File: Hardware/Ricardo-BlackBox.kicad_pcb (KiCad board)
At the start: 4 copper layers, 45.1 x 35.1 mm, 83 parts, among them J1 RBUS, J2 USB_C_Receptacle_USB2.0, J3 Conn_01x08_Pin, U1 ESP32-S3, U2 SN65HVD230, U3 LM66200DRLR, U4 MAX77827AEFD+T, U5 SC4215ASTRT, U7 LM66200DRLR, Y1 R940000171

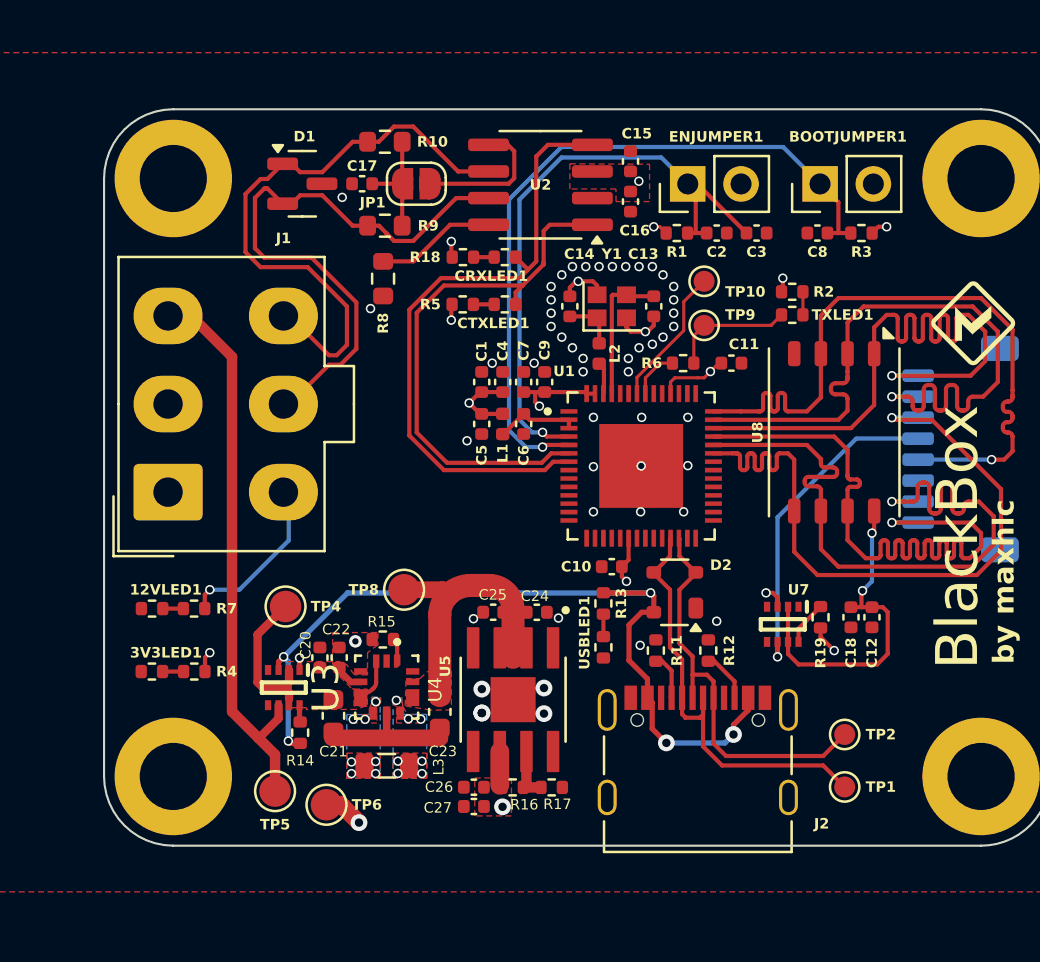
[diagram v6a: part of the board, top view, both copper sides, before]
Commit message: Update silkscreen labels for LEDs and pads
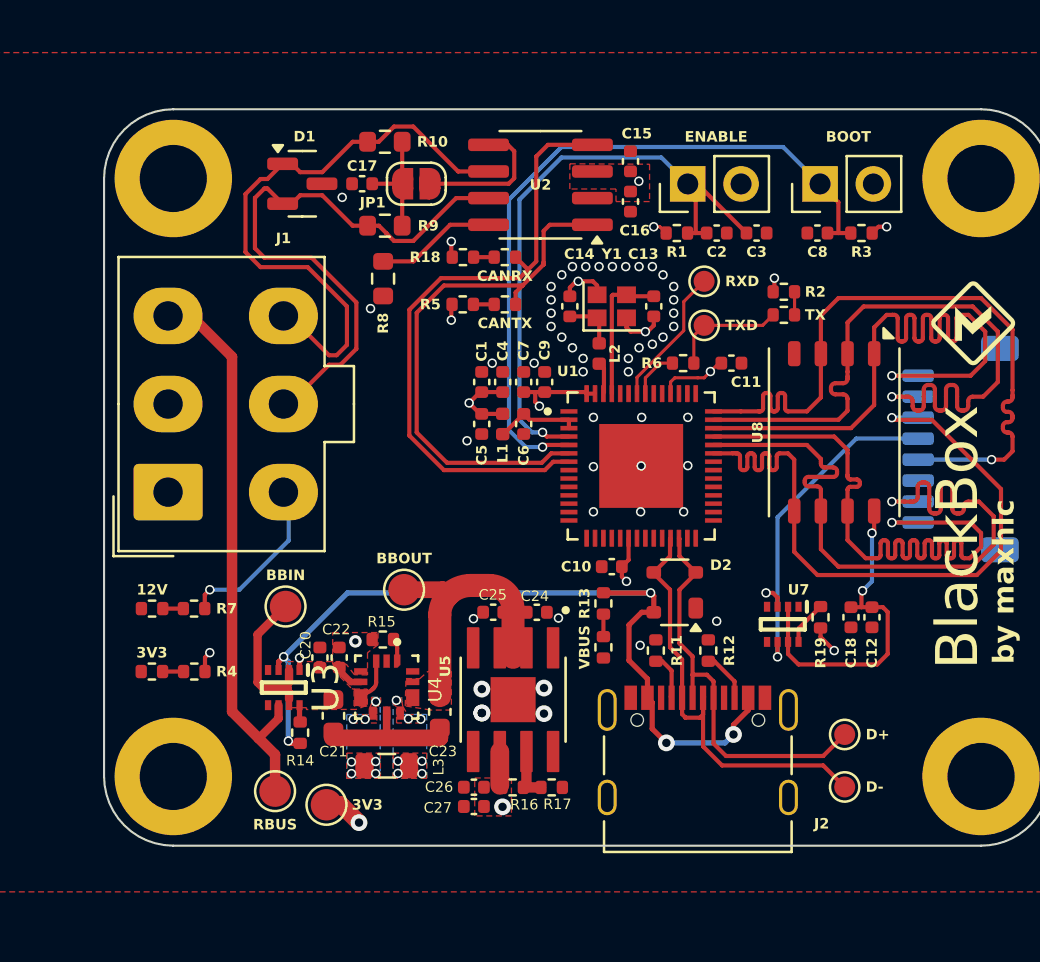
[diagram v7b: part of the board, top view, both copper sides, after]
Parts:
- moved R2 0.40 mm to (111.5, 54.5)
- moved TX 0.40 mm to (111.5, 55.6)
- renumbered 12VLED1 to 12V, TP6 to 3V3, 3V3LED1 to 3V3, TP4 to BBIN, TP8 to BBOUT, BOOTJUMPER1 to BOOT, CRXLED1 to CANRX, CTXLED1 to CANTX, TP2 to D+, TP1 to D-, ENJUMPER1 to ENABLE, TP5 to RBUS, TP10 to RXD, TXLED1 to TX, TP9 to TXD, USBLED1 to VBUS
